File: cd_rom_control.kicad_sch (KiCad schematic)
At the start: 13 parts, among them IC103 CXD1167Q, IC104 D78C14GF, IC105 D6378GF, IC106 D4364G, P401 Conn_01x10, P402 Conn_01x10, P404 Conn_01x08, P7 Conn_01x07

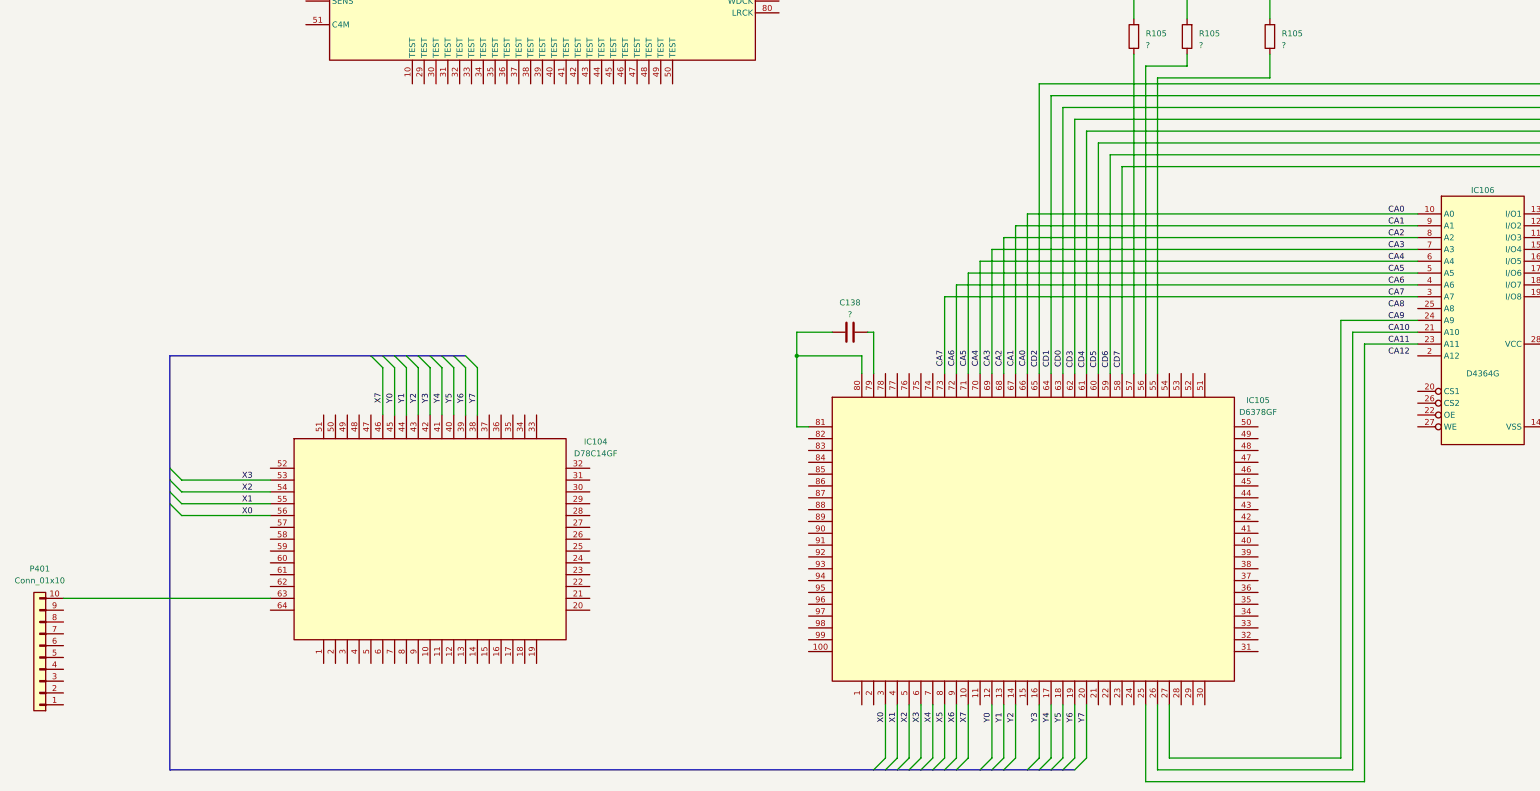
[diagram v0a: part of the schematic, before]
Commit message: Add proper scans, redo traces.
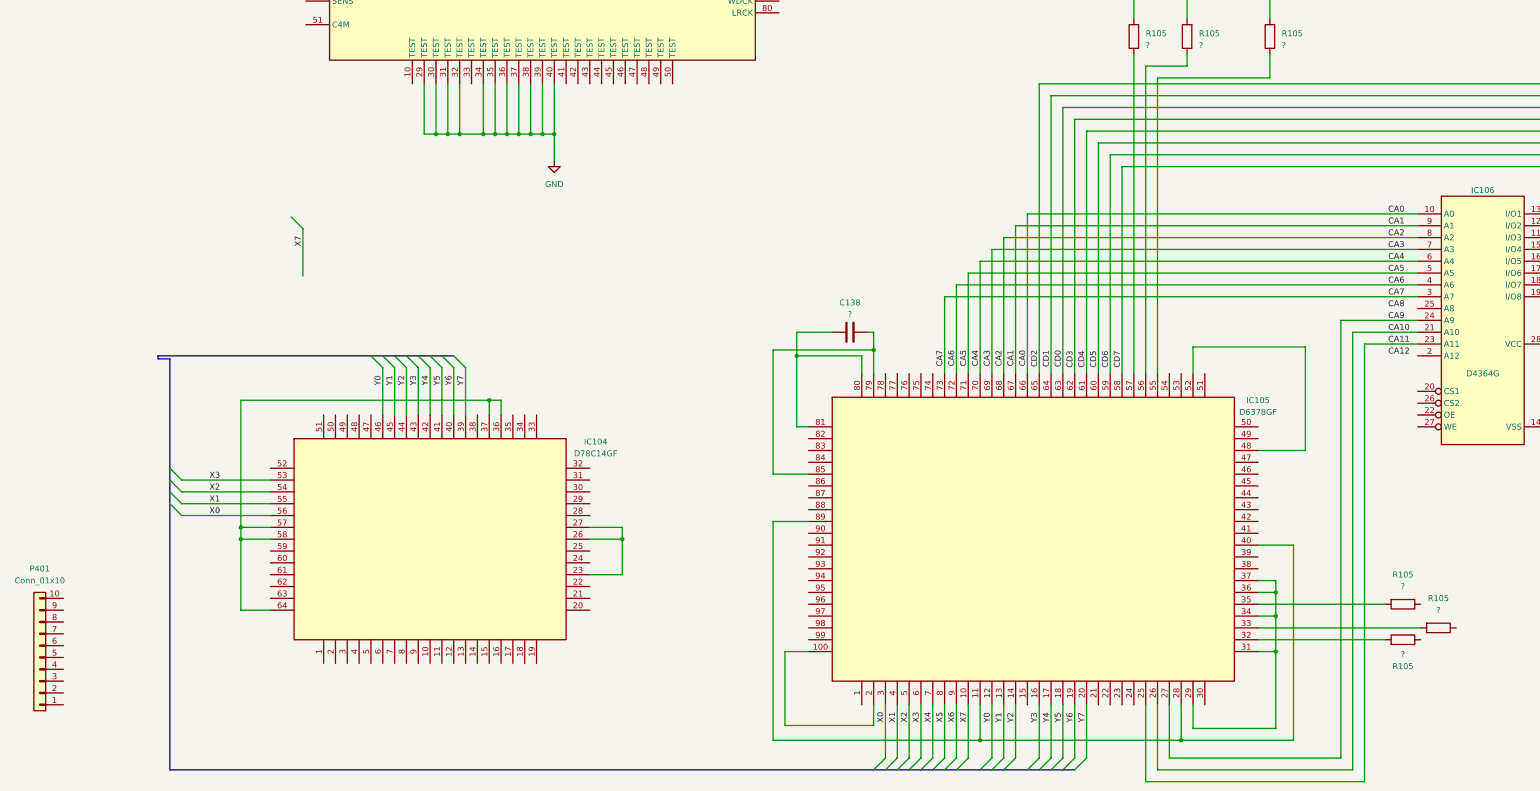
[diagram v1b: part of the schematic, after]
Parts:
- added R105 (x3): ?, Resistor_SMD:R_0805_2012Metric, symbol Device:R
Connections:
- net X7: no longer IC104.46
- net Y0: now also IC104.46; no longer IC104.45
- net Y1: now also IC104.45; no longer IC104.44
- net Y2: now also IC104.44; no longer IC104.43
- net Y3: now also IC104.43; no longer IC104.42
- net Y4: now also IC104.42; no longer IC104.41
- net Y5: now also IC104.41; no longer IC104.40
- net Y6: now also IC104.40; no longer IC104.39
- net Y7: now also IC104.39; no longer IC104.38
- net at IC105.100: now also IC105.2
- net at IC105.11: now also IC105.28, IC105.40, IC105.89
- net at IC105.29: now also IC105.31, IC105.34, IC105.36, IC105.37
- net at IC105.32: now also R105.2
- net at IC105.33: now also R105.2
- net at IC105.35: now also R105.2
- net at IC105.48: now also IC105.52
- net at C138.2, IC105.79: now also IC105.85
- net at P401.10 (Pin_10): no longer IC104.63
- net at IC104.23: now also IC104.26, IC104.27
- net at IC104.36: now also IC104.37, IC104.57, IC104.58, IC104.64
- net GND: now reaches IC103.29 (TEST)
- net GND: now also IC103.30 (TEST), IC103.31 (TEST), IC103.32 (TEST), IC103.34 (TEST), IC103.35 (TEST), IC103.36 (TEST), IC103.37 (TEST), IC103.38 (TEST), IC103.39 (TEST), IC103.40 (TEST)

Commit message: More tracing.
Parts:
- added R105 (x2): ?, Resistor_SMD:R_0805_2012Metric, symbol Device:R
- added RA502: R_Pack04, Resistor_SMD:R_Array_Concave_4x0603, symbol Device:R_Pack04
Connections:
- net X0: now also P401.3 (Pin_3); no longer IC104.56
- net X1: now also P401.4 (Pin_4); no longer IC104.55
- net X2: now also P401.5 (Pin_5); no longer IC104.54
- net X3: now also P401.6 (Pin_6); no longer IC104.53
- net X4: now also P401.7 (Pin_7)
- net X5: now also P401.8 (Pin_8)
- net X6: now also P401.9 (Pin_9)
- net X7: now also P401.10 (Pin_10)
- net Y3: now also IC105.15; no longer IC105.16
- net Y4: now also IC105.16; no longer IC105.17
- net Y5: now also IC105.17; no longer IC105.18
- net Y6: now also IC105.18; no longer IC105.19
- net Y7: now also IC105.19; no longer IC105.20
- net CFX2: now reaches R105.1
- net CFX0: now reaches R105.1
- net at IC105.35, R105.2: now also IC105.54
- net CFX1: now reaches R105.1
- net Y8: now reaches IC104.38
- net Y8: now also IC105.20
- net at IC103.10 (TEST): now also IC103.12 (VSS)
- net ATSC: now reaches IC103.2 (MON)
- net at IC103.26 (SQEX): now also IC103.33 (VDD)
- net TZC: now reaches IC103.3 (MDP)
- net at IC103.41 (TEST): now also IC103.42 (TEST), IC103.43 (TEST), IC103.44 (TEST), IC103.45 (TEST), IC103.46 (TEST), IC103.47 (TEST), IC103.48 (TEST), IC103.49 (TEST), IC103.50 (TEST), IC103.52 (VSS)
- net at IC103.55 (MD1): now also IC103.73 (?)
- net at IC103.56 (MD2): now also IC103.57 (MD3), IC103.59 (PSSL)
- net TE: now reaches IC103.7 (LOCK)
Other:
- moved on the sheet: P401

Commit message: Yet more tracing.
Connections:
- net DA10: now also P404.7 (Pin_7)
- net DA4: now also P404.5 (Pin_5)
- net GND: now also IC103.10 (TEST), IC103.12 (VSS), IC103.41 (TEST), IC103.42 (TEST), IC103.43 (TEST), IC103.44 (TEST), IC103.45 (TEST), IC103.46 (TEST), IC103.47 (TEST), IC103.48 (TEST), IC103.49 (TEST), IC103.50 (TEST), IC103.52 (VSS), RA502.5 (R4.2), RA502.6 (R3.2), RA502.7 (R2.2), RA502.8 (R1.2)
- net CFXR2: now reaches IC105.33, R105.2
- net CFX3: now reaches IC105.38
- net CFX4: now reaches IC105.39
- net CFX5: now reaches IC105.41
- net CFX6: now reaches IC105.42
- net CFX7: now reaches IC105.43
- net CFX8: now reaches IC105.44
- net CFX9: now reaches IC105.45
- net CFX10: now reaches IC105.46
- net CIF4: now reaches IC105.86
- net CIF4: now also RA502.3 (R3.1)
- net CIF3: now reaches IC105.88
- net CIF3: now also RA502.4 (R4.1)
- net GFS: now reaches P404.3 (Pin_3)
- net GFS: now also IC103.28 (GFS)
- net CRCF: now reaches P404.4 (Pin_4)
- net CRCF: now also IC103.20 (CRCF), IC104.62
- net MUTG: now reaches P404.8 (Pin_8)
- net MUTG: now also IC103.19 (MUTG)
- net SUBQ: now reaches IC104.12
- net SUBQ: now also IC103.23 (SUBQ)
- net SENS: now reaches IC104.16
- net SENS: now also IC103.18 (SENS)
- net DATA: now reaches IC104.19
- net DATA: now also IC103.15 (DATA)
- net SCOR: now reaches IC104.20
- net SCOR: now also IC103.24 (SCOR)
- net EXCK: now reaches IC103.21 (EXCK)
- net TG2: now reaches P7.3 (Pin_3)
- net TA-: now reaches P7.4 (Pin_4)
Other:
- moved on the sheet: RA502

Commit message: Power rails, etc.
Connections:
- net CA12: now also IC106.2 (A12)
- net CA8: now also IC106.25 (A8)
- net GND: now also IC105.11, IC105.28, IC105.40, IC105.53, IC105.89, IC106.14 (VSS), IC106.20 (CS1)
- net Y7: now also P402.5 (Pin_5)
- net at P402.1 (Pin_1): now also IC104.22
- net at P402.2 (Pin_2): now also IC104.8
- net at P402.3 (Pin_3): now also IC104.9
- net at P402.4 (Pin_4): now also IC104.10
- net at P402.6 (Pin_6): now also IC104.35
- net at P402.7 (Pin_7): now also IC104.34
- net at P402.9 (Pin_9): now also IC104.32
- net at IC106.26 (CS2): now also IC106.28 (VCC)
- net DVCC: now reaches IC104.15
- net FE0: now reaches IC104.18
- net XRST: now reaches IC104.2
- net XRST: now also IC103.16 (XRST)
- net FSW: now reaches IC104.6
- net CNIN: now reaches IC103.17 (CNIN)
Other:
- moved on the sheet: P402

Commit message: IC routing mostly complete, start adding passives.
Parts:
- removed R105: ?, Resistor_SMD:R_0805_2012Metric, symbol Device:R
- added C138 (x2): ?, A-PCENGINE:SMD_0805_Narrow, symbol Device:C
- added L106: ~, A-PCENGINE:SMD_0805_Narrow, symbol Device:L
- added R105 (x7): ?, A-PCENGINE:SMD_0805_Narrow, symbol Device:R
- added SW1: SW_Push, A-PCENGINE:SW_4Pin_3.25mm, symbol Switch:SW_Push
- added X101: Crystal, A-PCENGINE:L-5.00mm, symbol Device:Crystal
- C138: footprint Capacitor_SMD:C_0805_2012Metric -> A-PCENGINE:SMD_0805_Narrow
- R105: footprint Resistor_SMD:R_0805_2012Metric -> A-PCENGINE:SMD_0805_Narrow
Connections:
- net CA10: now also IC105.27, R105.2; no longer IC105.26
- net CA11: now also IC105.26, R105.2; no longer IC105.25
- net CA12: now also IC105.25, R105.2
- net CA8: now also IC105.74
- net CA9: now also IC105.30, R105.2; no longer IC105.27
- net CIF3: now also IC104.17; no longer IC105.88, RA502.4 (R4.1)
- net DVCC: now also IC103.13 (CLK)
- net FE0: now also P404.1 (Pin_1)
- net FSW: now also IC103.14 (XLT)
- net GND: now also P3.2 (Pin_2), C138.1, C138.1
- net MUTG: now also IC104.11
- net Y0: now also P402.10 (Pin_10)
- net DX: now reaches IC104.22, P402.1 (Pin_1)
- net DX: now also IC105.49, IC105.99
- net P7P2: now reaches IC104.8, P402.2 (Pin_2)
- net P7P2: now also P7.2 (Pin_2)
- net P3P4: now reaches IC104.35, P402.6 (Pin_6)
- net LID_B: now reaches P402.8 (Pin_8)
- net LID_B: now also P7.1 (Pin_1), SW1.2
- net CWE: now reaches IC105.21
- net CWE: now also IC106.27 (WE), R105.1
- net at IC105.75: now also R105.1
- net at IC105.76: now also R105.1
- net at IC105.77: now also R105.1
- net at IC105.78: now also R105.1
- net COE: now reaches IC105.83
- net COE: now also IC106.22 (OE)
- net at IC105.84: now also R105.2
- net BCLK: now reaches IC105.87
- net XCLK: now reaches IC105.90
- net XCLK: now also IC103.54 (XTAO), C138.2, R105.2, X101.2
- net KAK2: now reaches IC105.94
- net KAK2: now also IC104.59
- net KAK1: now reaches IC105.95
- net KAK1: now also IC104.60
- net KAK0: now reaches IC105.96
- net KAK0: now also IC104.61
- net CIF5: now reaches RA502.1 (R1.1)
- net CIF6: now reaches RA502.2 (R2.1)
- net +5VD: now reaches IC106.26 (CS2), IC106.28 (VCC)
- net +5VD: now also L106.1, L106.2
- net TGU: now reaches P404.2 (Pin_2)
- net P404P6: now reaches P404.6 (Pin_6)
- net MDS: now reaches R105.2
- net MDS: now also IC103.4 (MDS)
- net SQCK: now reaches IC104.13
- net SQCK: now also IC103.25 (SQCK)
- net MD2: now reaches IC104.3
- net MD2: now also IC103.56 (MD2), IC103.57 (MD3), IC103.59 (PSSL)
- net ACTIVE: now reaches IC104.63
- net FSW2: now reaches IC103.1 (FSW)
- net EFM: now reaches IC103.5 (EFM)
- net at IC103.53 (XTAI): now also R105.2
- net ASY: now reaches IC103.6 (ASY)
- net P7P5: now reaches P7.5 (Pin_5)
- net P7P6: now reaches P7.6 (Pin_6)
- net SL+: now reaches P7.7 (Pin_7)
- net DATA renamed MON
- new net: C138.2, R105.1, R105.1, X101.1
- new net LID_A: SW1.1
- new net LRCK: IC105.88, RA502.4 (R4.1)
- no-connect marks 0 -> 3
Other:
- moved on the sheet: IC103, IC106, P3, P404, P7, R105

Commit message: Bunch of passives and what-not.
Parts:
- removed R105: ?, A-PCENGINE:SMD_0805_Narrow, symbol Device:R
- added D102: ~, A-PCENGINE:Transistor_SMD, symbol Device:D_Dual_CommonCathode_KAA
- added TP7 (x2): ~, A-PCENGINE:Test_Point_1.5mm, symbol Connector:TestPoint
- C138, R105: footprint A-PCENGINE:SMD_0805_Narrow -> A-PCENGINE:SMD_0805_Narrow_Long
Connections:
- net FSW2 is gone; now on net FSW: IC103.1 (FSW)
- net P7P2 is gone; now on net LID_A: IC104.8, P402.2 (Pin_2), P7.2 (Pin_2)
- net SL+ is gone; now on net ATSC: P7.7 (Pin_7)
- net TG2 is gone; now on net TE: P7.3 (Pin_3)
- net +5VD: now also C138.2, IC103.26 (SQEX), IC103.33 (VDD), IC103.55 (MD1), IC103.73 (?), IC105.100, IC105.2, IC105.29, IC105.31, IC105.34, IC105.36, IC105.37, IC105.48, IC105.52, IC105.79, IC105.85, IC105.91
- net ATSC: no longer IC103.2 (MON)
- net FSW: no longer IC103.14 (XLT), IC104.6
- net GND: now also C138.1, IC103.58 (SLOB), IC105.1, IC105.80, IC105.81, IC105.98
- net LID_A: now also D102.1 (K); no longer SW1.1
- net LID_B: now also TP7.1
- net MON: now also IC103.2 (MON); no longer IC103.15 (DATA), IC104.19
- net TE: no longer IC103.7 (LOCK)
- net KAK3: now reaches IC105.93
- net PDO: now reaches IC103.11 (PDO)
- net VCOO: now reaches IC103.8 (VCOO)
- net VCOI: now reaches IC103.9 (VCOI)
- net FE0 renamed FOK
- net TA- renamed FE
- net TGU renamed DFCT
- net TZC renamed MDP
- new net: D102.2 (A), SW1.1, TP7.1
- new net DATA: IC103.15 (DATA), IC104.19
- new net LOCK: IC103.7 (LOCK)
- new net P3P3: D102.3 (A)
- new net XLT: IC103.14 (XLT), IC104.6
- no-connect marks 3 -> 9

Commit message: More passives, custom footprints, etc.
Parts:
- added C105: ?, A-PCENGINE:CP_6x1.5mm, symbol Device:C_Polarized
- added C138 (x2): ?, A-PCENGINE:SMD_0805_Narrow_Long, symbol Device:C
- added CF101: 12.0, A-PCENGINE:CF_4.4x7.8, symbol Device:Crystal
- added R105 (x4): ?, A-PCENGINE:SMD_0805_Narrow_Long, symbol Device:R
- added TP1, TP2, TP3, TP4, TP5 (x2), TP6 (x2), TP7 (x2): ~, A-PCENGINE:Test_Point_1.5mm, symbol Connector:TestPoint
- P402: value Conn_01x10 -> ~
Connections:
- net +5VD: now also IC104.36, IC104.37, IC104.57, IC104.58, IC104.64, C105.1, R105.2
- net DX: now also TP1.1
- net GND: now also IC104.23, IC104.26, IC104.27, C105.2, C138.2, C138.2, R105.2, R105.2, R105.2
- net LID_A: now also R105.1, TP2.1
- net LID_B: now also TP5.1
- net P3P4: now also TP6.1
- net Y0: now also TP7.1
- net Y7: now also R105.1, TP5.1
- net at IC104.9, P402.3 (Pin_3): now also R105.1, TP3.1
- net at IC104.10, P402.4 (Pin_4): now also R105.1, TP4.1
- net at IC104.34, P402.7 (Pin_7): now also TP7.1
- net at IC104.32, P402.9 (Pin_9): now also TP6.1
- net at IC104.24: now also C138.1, CF101.2
- net at IC104.25: now also C138.1, CF101.1
- no-connect marks 9 -> 15
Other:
- moved on the sheet: IC104, P401, P402, R105

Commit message: Top layer first draft.
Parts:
- added C138 (x3): ?, A-PCENGINE:SMD_0805_Narrow_Long, symbol Device:C
- added C138: ?, A-PCENGINE:SMD_0805_Narrow, symbol Device:C
- added C951 (x2): ~, A-PCENGINE:CP_6x1.5mm, symbol Device:C_Polarized
- added C951: ?, A-PCENGINE:CP_6x1.5mm, symbol Device:C_Polarized
- added C951 (x2): ~, A-PCENGINE:CP_7x2mm, symbol Device:C_Polarized
- added Q1, Q102: Q_NPN_CBE, A-PCENGINE:Transistor_SMD, symbol Device:Q_NPN_CBE
- added Q203, Q204: 15 29, A-PCENGINE:Transistor_SMD, symbol Device:Q_PNP_CBE
- added R105 (x8): ?, A-PCENGINE:SMD_0805_Narrow_Long, symbol Device:R
- added R105 (x2): ?, A-PCENGINE:SMD_0805_Narrow, symbol Device:R
- added TP7: ~, A-PCENGINE:Test_Point_1.5mm, symbol Connector:TestPoint
- IC103: footprint Package_QFP:PQFP-80_14x20mm_P0.8mm -> A-PCENGINE:PQFP-80_P0.8mm
- IC105: footprint Package_QFP:PQFP-100_14x20mm_P0.65mm -> A-PCENGINE:PQFP-100_P0.65mm
- P3: footprint Connector_PinHeader_2.00mm:PinHeader_1x02_P2.00mm_Vertical -> A-PCENGINE:Header_1x02_P2.00mm
- P401, P402: footprint Connector_PinHeader_2.00mm:PinHeader_1x10_P2.00mm_Vertical -> A-PCENGINE:Header_1x10_P2.00mm
- P404: footprint Connector_PinHeader_2.00mm:PinHeader_1x08_P2.00mm_Vertical -> A-PCENGINE:Header_1x08_P2.00mm_Narrow
- P7: footprint Connector_PinHeader_2.00mm:PinHeader_1x07_P2.00mm_Vertical -> A-PCENGINE:Header_1x07_P2.00mm
- RA502: footprint Resistor_SMD:R_Array_Concave_4x0603 -> A-PCENGINE:R_Array_4x0603
- renumbered SW1 to SW401
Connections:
- net +5VD: now also P401.2 (Pin_2), C138.2, C951.1, C951.1, C951.1, C951.1, C951.1, Q203.3 (E), Q204.3 (E), R105.1, R105.2, R105.2
- net DATA: now also Q204.1 (C)
- net DX: now also C138.1
- net GFS: now also R105.1
- net GND: now also P401.1 (Pin_1), C138.1, C138.1, C138.2, C138.2, C951.2, C951.2, C951.2, C951.2, C951.2, Q1.3 (E), Q102.3 (E), R105.1, R105.2, R105.2, R105.2, R105.2
- net KAK3: now also Q1.2 (B)
- net LID_B: now also R105.1
- net MUTG: now also R105.1
- net P3P4: now also R105.1
- net at IC104.34, P402.7 (Pin_7), TP7.1: now also R105.1
- net at IC104.32, P402.9 (Pin_9), TP6.1: now also R105.1
- net at IC104.14: now also Q1.1 (C), R105.2
- net at IC104.21: now also R105.1
- net at IC104.33: now also C138.2, R105.1, R105.2
- net at IC104.4: now also Q203.2 (B)
- net at IC104.7: now also Q204.2 (B), TP7.1
- new net: C138.1, Q102.2 (B), R105.2
- new net: Q102.1 (C), R105.2
